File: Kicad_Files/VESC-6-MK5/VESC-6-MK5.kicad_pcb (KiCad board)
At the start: 4 copper layers, 105.9 x 102.5 mm, 151 parts, among them P1 USB_OTG, P10 PH_C, P11 SUPPLY, P12 GND, P2 CAN, P4 HALL_ENC, P5 COMM, P6 SERVO, P7 SWD, P8 PH_A, P9 PH_B, Q1 IRF7749, Q2 IRF7749, Q3 IRF7749, Q4 IRF7749, Q5 IRF7749, Q6 IRF7749, Q7 DMN62D0UW-7, U1 STM32F405RGTx, U10 MC74VHC1GT66, U11 SENS_VOLT, U12 MC74VHC1GT66, U13 MC74VHC1GT66, U14 MC74VHC1GT66DF1G, U15 MC74VHC1GT66DF1G, U16 MC74VHC1GT66DF1G, U3 DRV8301DCA, U4 TJA1051TK-3, U5 AD8418, U6 AD8418, U7 AD8418, U8 TC2117-3.3VEBTR, U9 BMI160, Y1 8M

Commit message: Switched stunt resistors location
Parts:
- R24, R29, R32: moved to F.Cu
- moved C46 58.2 mm to (208.1, 46.6), turned to 90 degrees
- moved C47 58.2 mm to (208.3, 60.9), turned to 90 degrees
- moved R24 23.3 mm to (166.2, 74.3), turned to 90 degrees
- moved R29 21.9 mm to (179.9, 74.2), turned to 90 degrees
- moved R32 21.5 mm to (192.8, 74.2), turned to 90 degrees
- moved Q7 12.1 mm to (168.9, 104.9)
- moved R15 12.1 mm to (171.2, 105.0)
- moved R16 12.1 mm to (166.6, 105.0)
- moved Q5 9.34 mm to (191.1, 64.7)
- moved C37 9.33 mm to (171.4, 56.7)
- moved C39 9.33 mm to (175.1, 56.7)
- moved C40 9.33 mm to (178.9, 56.7)
- moved C41 9.33 mm to (182.6, 56.7)
- moved C43 9.33 mm to (186.4, 56.7)
- moved C44 9.33 mm to (190.1, 56.7)
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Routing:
- net Net-(P8-Pin_1): track 13.6 -> 210.7 mm, vias 31 -> 43
- net GNDPWR: track 135.5 -> 183.8 mm
- net SUPPLY: track 260.7 -> 306.9 mm
- net Net-(P9-Pin_1): track 13.0 -> 46.2 mm
- net /SH_A: track 184.6 -> 216.9 mm
- net Net-(U5-IN+): track 7.89 -> 37.8 mm, vias 1 -> 2
- net Net-(U6-IN+): track 6.92 -> 36.8 mm, vias 1 -> 2
- net Net-(P10-Pin_1): track 11.1 -> 40.4 mm
- net Net-(U5-IN-): track 7.65 -> 29.0 mm, vias 1 -> 0
- net Net-(U6-IN-): track 8.23 -> 28.6 mm, vias 1 -> 0
- net Net-(U7-IN+): track 13.9 -> 33.1 mm, vias 1 -> 2
- net Net-(Q1-G): track 47.0 -> 65.4 mm, vias 5 -> 3
- net Net-(U7-IN-): track 7.76 -> 22.6 mm
- net /DRV8301/SH_C: track 133.8 -> 146.5 mm, vias 11 -> 10
- net /DRV8301/SENS_SUPPLY: track 79.8 -> 69.3 mm
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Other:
- board size 105.9 x 102.5 mm -> 105.8 x 114.1 mm

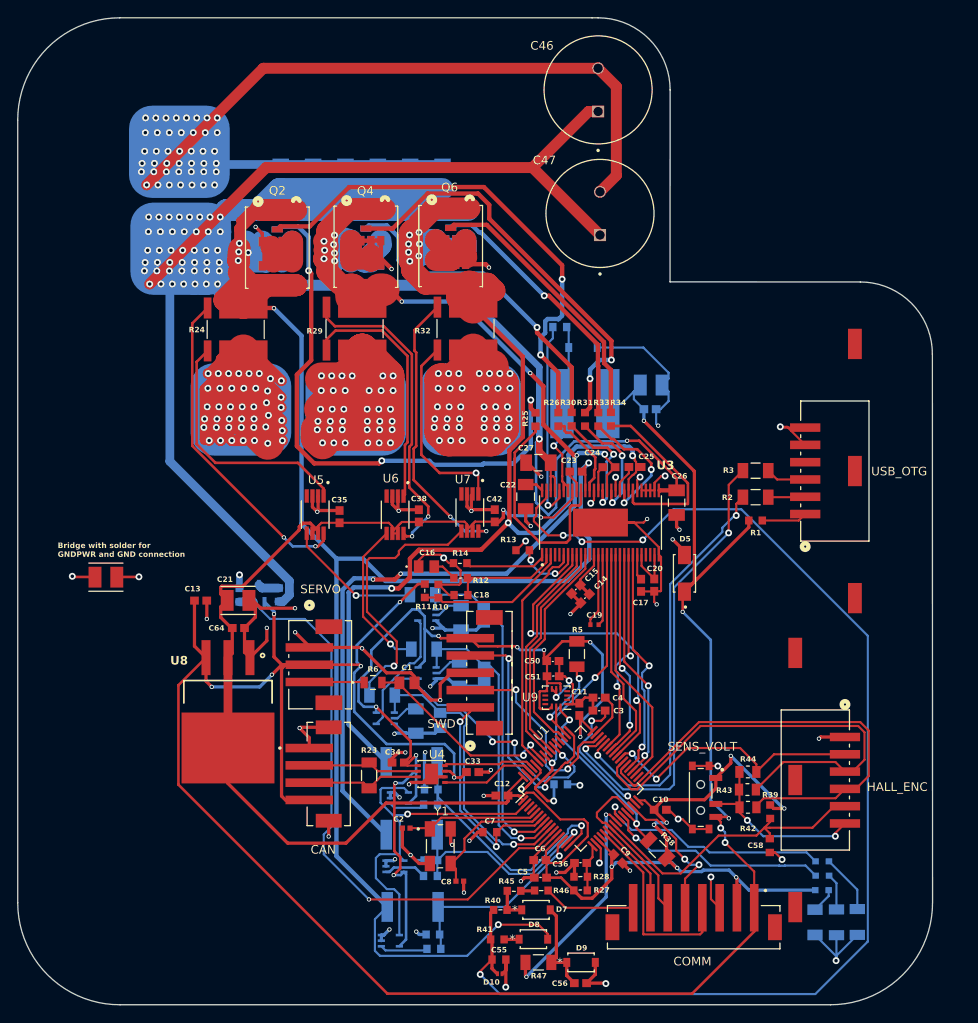
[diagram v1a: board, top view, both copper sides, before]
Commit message: Moved current sense amplifiers next to the shunt resistors
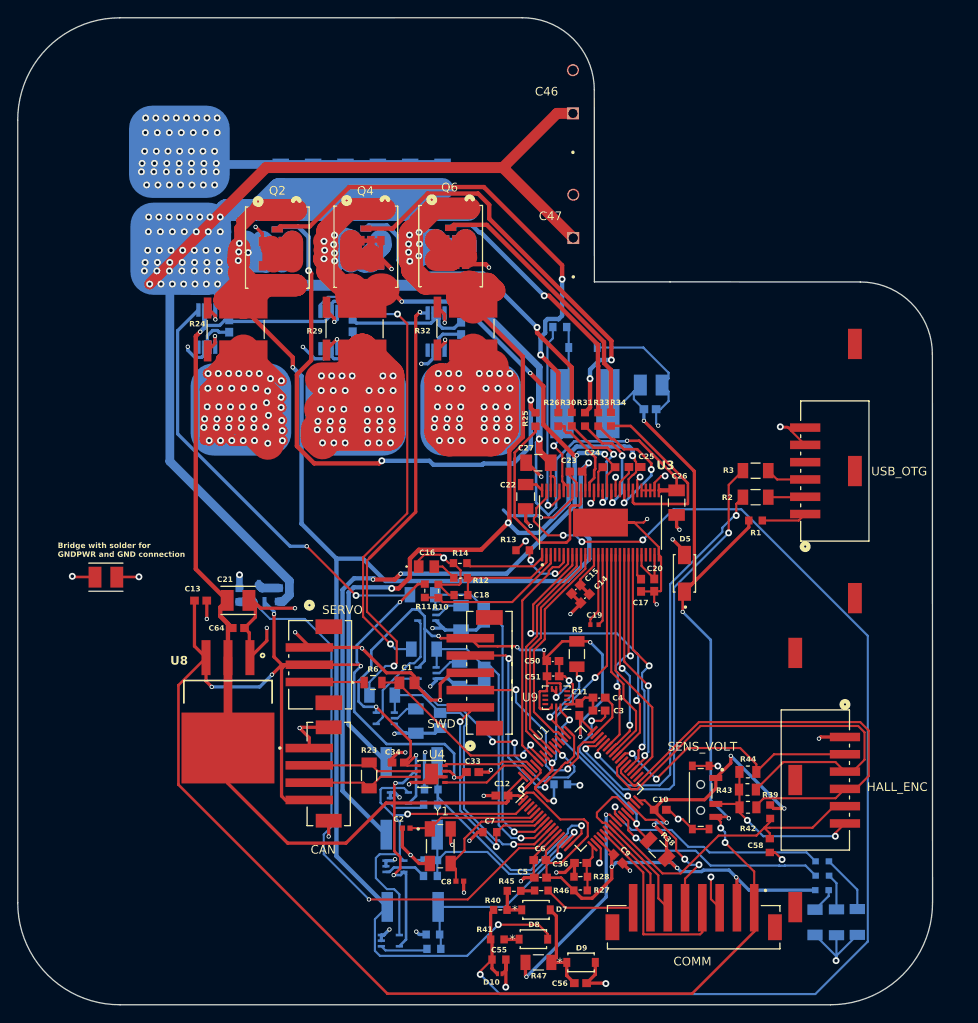
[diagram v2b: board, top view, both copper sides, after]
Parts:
- C35, C38, C42, U5, U6, U7: moved to B.Cu
- moved C35 25.5 mm to (165.4, 73.9), turned to 90 degrees
- moved U5 24.9 mm to (162.8, 74.2), turned to 90 degrees
- moved C38 23.3 mm to (179.7, 73.9), turned to 90 degrees
- moved U6 22.7 mm to (177.0, 74.4), turned to 90 degrees
- moved C42 22.0 mm to (192.3, 74.2), turned to 90 degrees
- moved U7 21.3 mm to (189.4, 74.6), turned to 90 degrees
- moved C47 3.11 mm to (205.2, 61.3)
- moved C46 2.92 mm to (205.2, 46.8)
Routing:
- net GNDPWR: track 183.8 -> 116.5 mm
- net /Power/C_B: track 17.9 -> 55.7 mm, vias 1 -> 2
- net Net-(U5-IN+): track 37.8 -> 2.80 mm, vias 2 -> 1
- net /Power/C_A: track 15.8 -> 50.0 mm, vias 1 -> 2
- net Net-(U6-IN+): track 36.8 -> 3.08 mm, vias 2 -> 1
- net Net-(U7-IN+): track 33.1 -> 3.27 mm, vias 2 -> 1
- net VCC: track 343.8 -> 371.6 mm
- net Net-(U5-IN-): track 29.0 -> 3.38 mm, vias 0 -> 1
- net Net-(U6-IN-): track 28.6 -> 3.26 mm, vias 0 -> 1
- net Net-(U7-IN-): track 22.6 -> 2.80 mm
- net /Power/C_C: track 31.4 -> 51.1 mm, vias 1 -> 2
- net SUPPLY: track 306.9 -> 304.3 mm
- net /SH_A: track 216.9 -> 214.9 mm
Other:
- board size 105.8 x 114.1 mm -> 105.8 x 114.2 mm

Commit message: Added mounting hardware
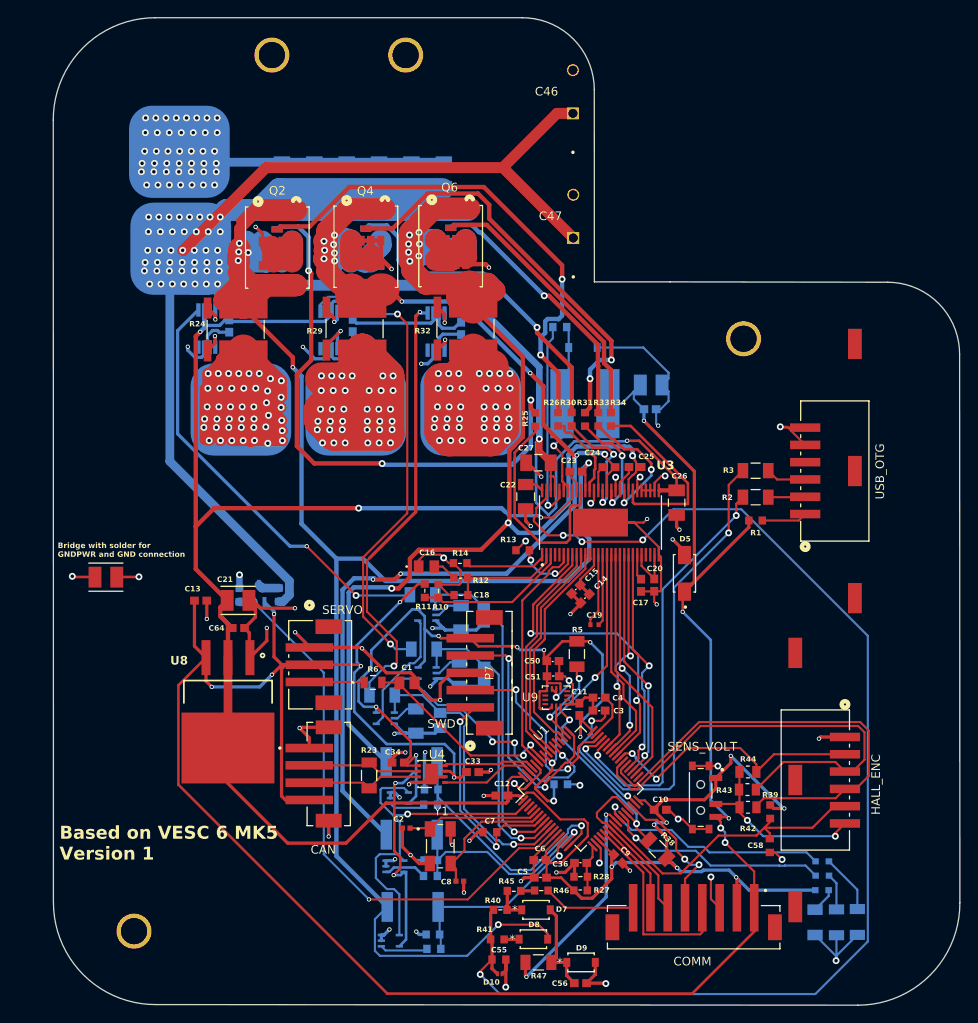
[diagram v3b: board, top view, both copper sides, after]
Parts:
- added ?: , , F.Cu at (154.4, 143.9)
- added ?: , , F.Cu at (224.9, 75.4)
- added ?: , , F.Cu at (185.8, 42.6)
- added ?: , , F.Cu at (170.4, 42.6)
- moved C37 0.30 mm to (171.5, 56.4)
- moved C44 0.30 mm to (190.3, 56.4)
- moved C39 0.30 mm to (175.3, 56.4)
- moved C40 0.30 mm to (179.0, 56.4)
- moved C41 0.30 mm to (182.8, 56.4)
- moved C43 0.30 mm to (186.5, 56.4)
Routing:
- net VCC: track 371.6 -> 409.2 mm, vias 18 -> 19
- net Net-(P8-Pin_1): track 210.7 -> 227.2 mm
- net SUPPLY: track 304.3 -> 298.9 mm
- net /DRV8301/SENS_SUPPLY: track 69.3 -> 66.2 mm
- net Net-(U6-IN-): track 3.26 -> 5.48 mm
- net GNDPWR: track 116.5 -> 118.6 mm
- net GND: track 248.8 -> 249.9 mm
- net Net-(P9-Pin_1): track 46.2 -> 47.3 mm
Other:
- board size 105.8 x 114.2 mm -> 104.8 x 114.2 mm
- board text added: "Based on VESC 6 MK5 Version 1"

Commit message: Working sample of the display
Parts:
- removed C60: 100u, DRV8301_:CAP_TPS1210_3P5X2P8_AVX
- U11: value SENS_VOLT -> SENSOR_VOLTAGE
- turned C16 to 90 degrees
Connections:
- C29 pad 2: GNDPWR -> GND
- C30 pad 2: GNDPWR -> GND
- C35 pad 1: GNDPWR -> GND
- C37 pad 1: GNDPWR -> GND
- C38 pad 1: GNDPWR -> GND
- C39 pad 1: GNDPWR -> GND
- C40 pad 1: GNDPWR -> GND
- C41 pad 1: GNDPWR -> GND
- C42 pad 1: GNDPWR -> GND
- C43 pad 1: GNDPWR -> GND
- C44 pad 1: GNDPWR -> GND
- C45 pad 2: GNDPWR -> GND
- C46 pad 2: GNDPWR -> GND
- C47 pad 2: GNDPWR -> GND
- C52 pad 2: GNDPWR -> GND
- C53 pad 2: GNDPWR -> GND
- C54 pad 2: GNDPWR -> GND
- P12 pad 1: GNDPWR -> GND
- Q2 pad 8: GNDPWR -> GND
- Q4 pad 8: GNDPWR -> GND
- Q6 pad 8: GNDPWR -> GND
- U10 pad 3: GNDPWR -> GND
- U12 pad 3: GNDPWR -> GND
- U13 pad 3: GNDPWR -> GND
- U3 pad 34: GNDPWR -> GND
- U3 pad 39: GNDPWR -> GND
- U3 pad 44: GNDPWR -> GND
- U5 pad 2: GNDPWR -> GND
- U5 pad 3: GNDPWR -> GND
- U6 pad 2: GNDPWR -> GND
- U6 pad 3: GNDPWR -> GND
- U7 pad 2: GNDPWR -> GND
- U7 pad 3: GNDPWR -> GND
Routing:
- net GNDPWR: track 118.6 -> 0.00 mm, vias 56 -> 0
- net GND: track 249.9 -> 363.3 mm, vias 51 -> 105
- net /Power/C_A: track 50.0 -> 58.1 mm
- net SUPPLY: track 298.9 -> 305.3 mm
- net VCC: track 409.2 -> 414.2 mm
- net /SH_A: track 214.9 -> 216.6 mm
- added copper zone on In2.Cu, net GND
- removed copper zone on In2.Cu, net GNDPWR
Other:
- board text removed: "Bridge with solder for GNDPWR and GND connection"
